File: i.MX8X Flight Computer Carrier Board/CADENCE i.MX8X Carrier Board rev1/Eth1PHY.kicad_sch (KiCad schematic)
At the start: 63 parts, among them Q1 IRLML6401, Q2 BSS138, U13 DP83867IRRGZR, U14 74LVC2G07, Y1 25MHz

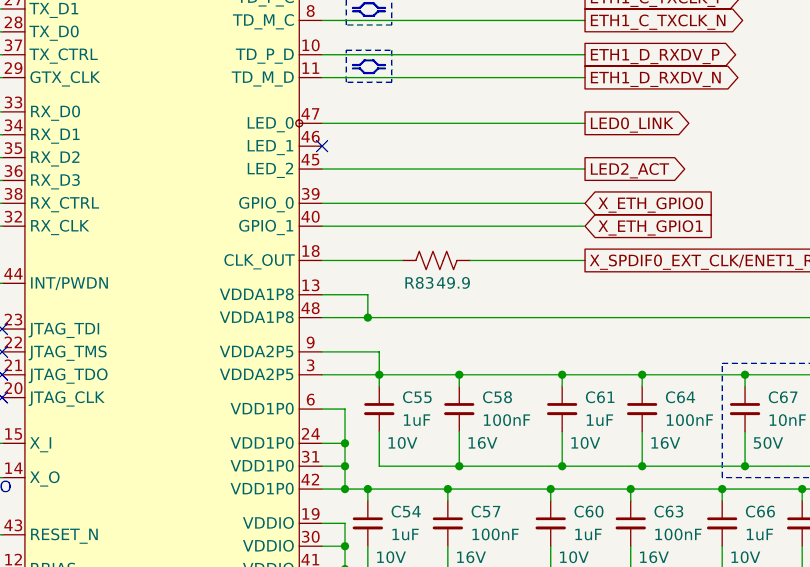
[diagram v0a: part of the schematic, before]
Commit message: BOM part selection, DRC fixes for traces & shorted vias, fixed power pours mentioned in previous design review
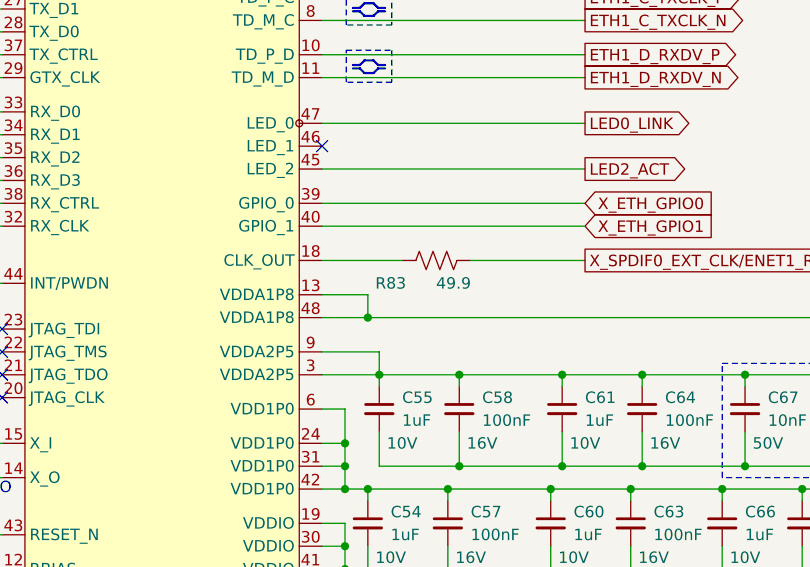
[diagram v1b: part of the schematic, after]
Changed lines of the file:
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@@
 		(dnp no)
 		(property "Reference" "R83"
-			(at 192.405 96.52 90)
+			(at 189.23 96.52 90)
 			(effects
 				(font
